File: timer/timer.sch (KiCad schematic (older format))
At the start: 1 part, among them P1 CONN_02X30

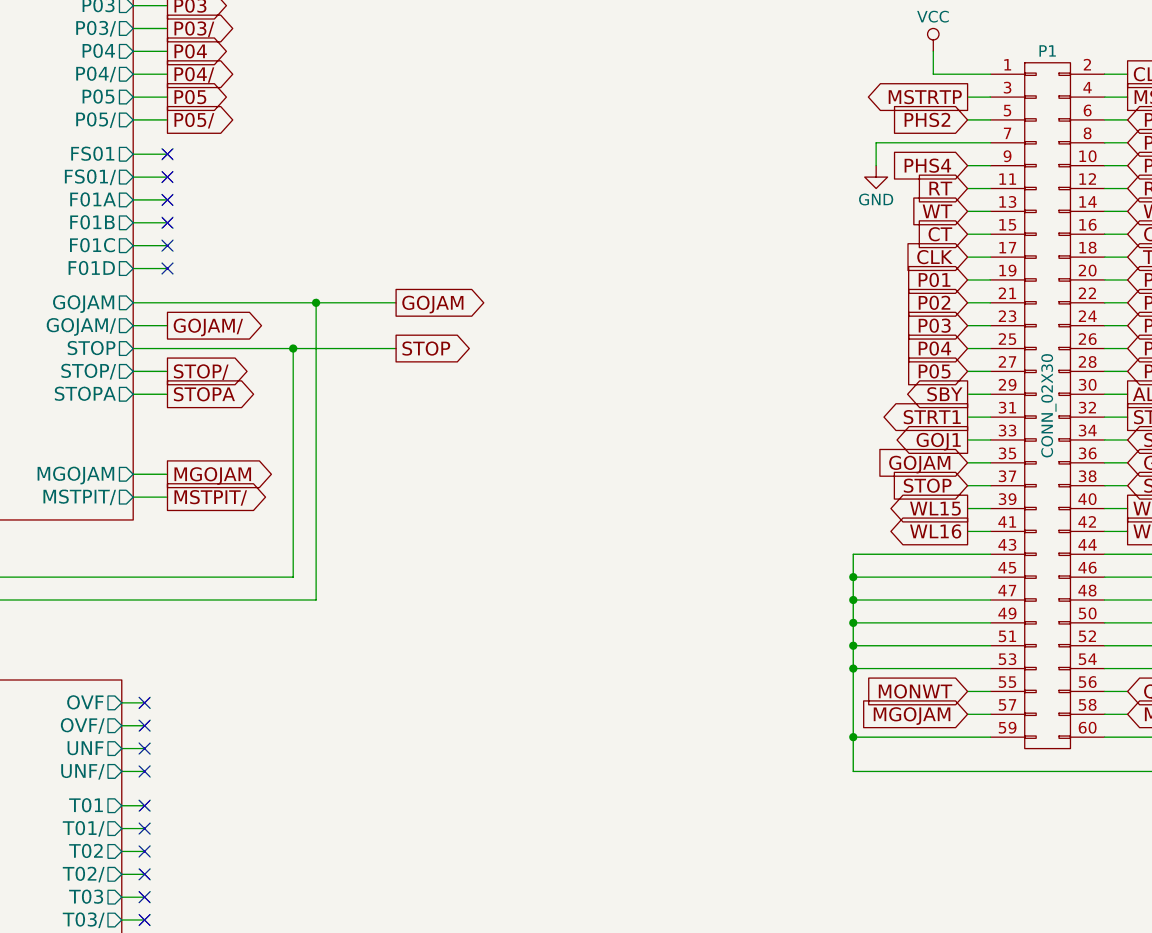
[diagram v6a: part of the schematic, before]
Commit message: Added the entire scaler module! Didn't flesh out the I/O much, I'll do that as needed. Also, the clock divider's labeling here is different from the one in the timer module, which is consistent with the original schematics. If I merge these two modules later, I'll have to figure out what to do there.
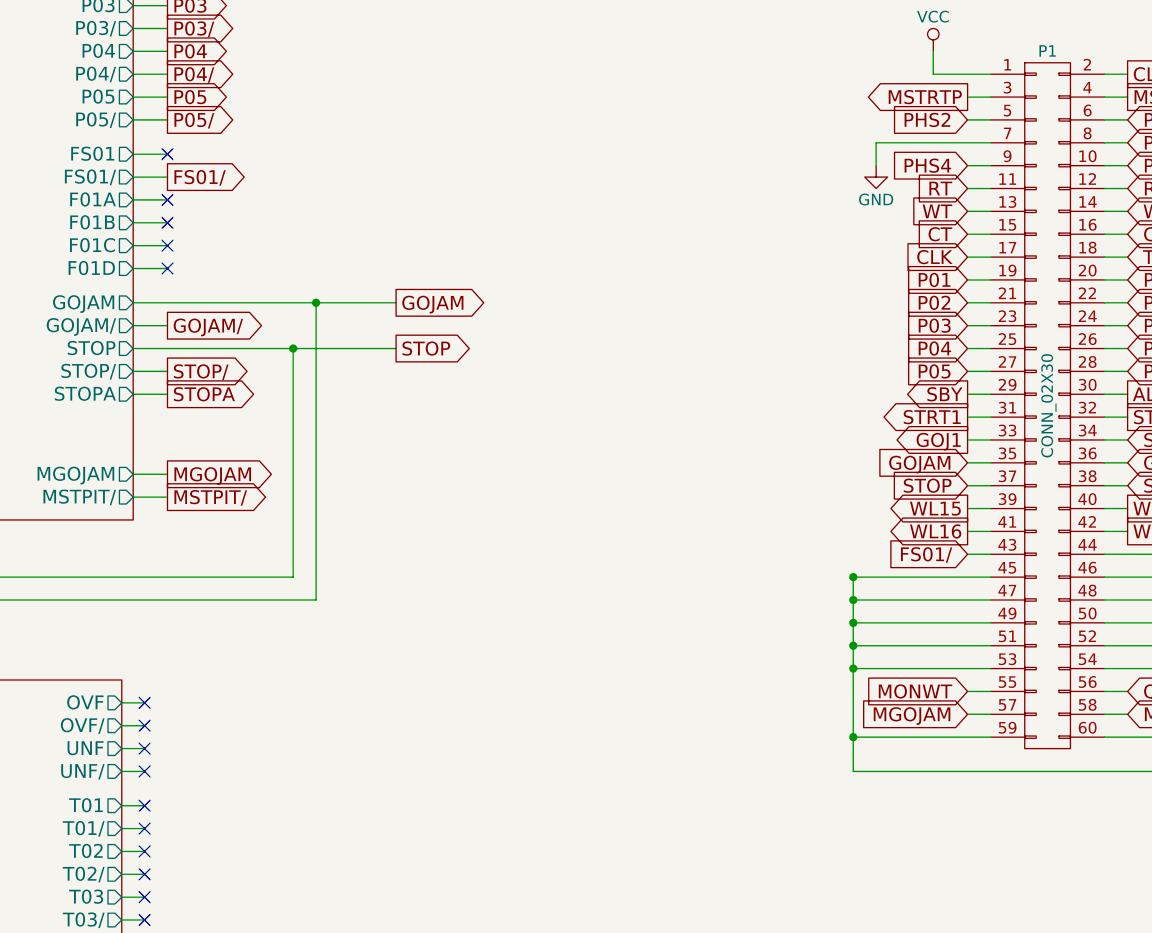
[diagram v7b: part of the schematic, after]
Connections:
- net GND: no longer P1.43 (P43)
- new net FS01/: P1.43 (P43)
- no-connect marks 58 -> 57
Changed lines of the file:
@@
 	6400 2850 6550 2850
 NoConn ~ 6550 2350
-NoConn ~ 6550 2450
 NoConn ~ 6550 2550
 NoConn ~ 6550 2650
@@
 	11300 4900 10650 4900
 Connection ~ 11300 4900
-Wire Wire Line
-	10150 4100 9550 4100
 Wire Wire Line
 	10150 4200 9550 4200
@@
 NoConn ~ 6450 5050
 Wire Wire Line
-	9550 5050 9550 4100
-Wire Wire Line
 	11300 4100 11300 5100
 Text GLabel 10050 3900 0    60   Output ~ 0
@@
 Wire Wire Line
 	4550 5900 4700 5900
+Wire Wire Line
+	9550 5050 9550 4200
+Wire Wire Line
+	10150 4100 10050 4100
+Text GLabel 10050 4100 0    60   Input ~ 0
+FS01/
+Text GLabel 6550 2450 2    60   Output ~ 0
+FS01/
 $EndSCHEMATC

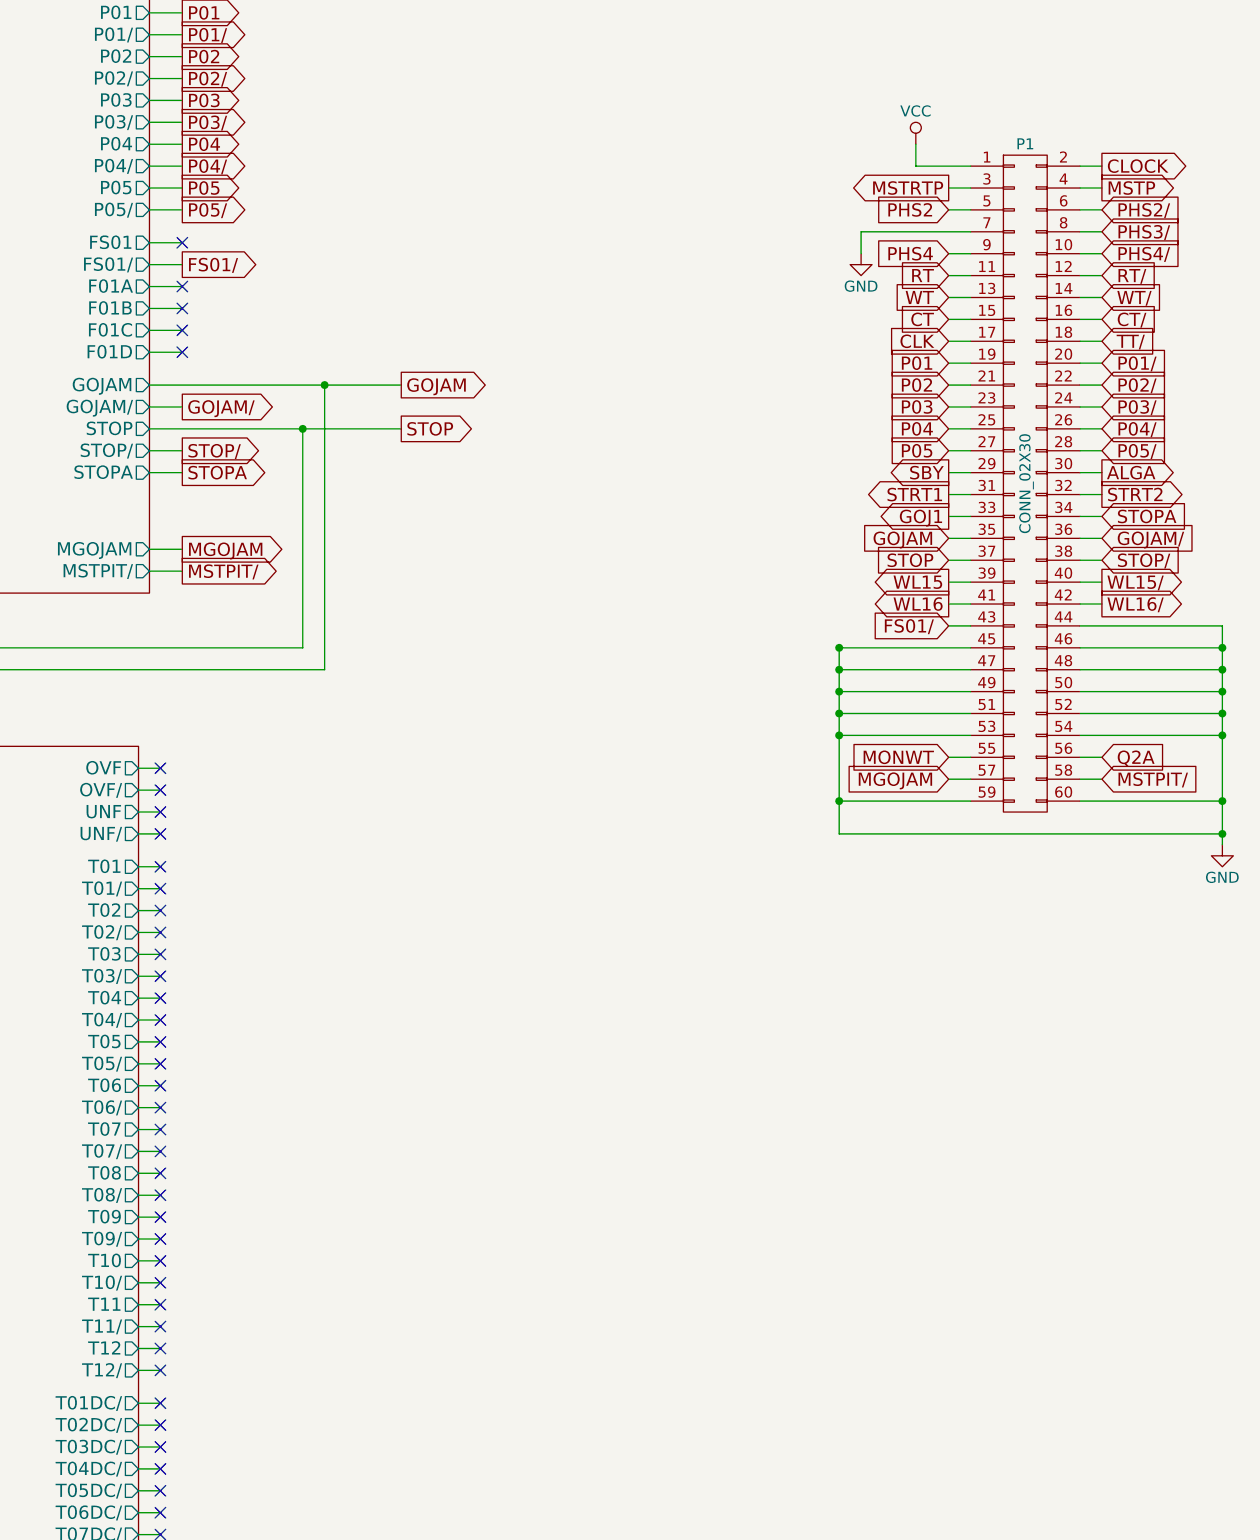
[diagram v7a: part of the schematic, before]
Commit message: Filled out the rest of page A03-1. At the very least, it appears to be properly handling the GOJAM condition. Haven't looked much at non-GOJAM behavior. I also exposed T01..T12 and T01/..T12/ as outputs of the timer module. I'm going to need a bigger (or another) connector there soon
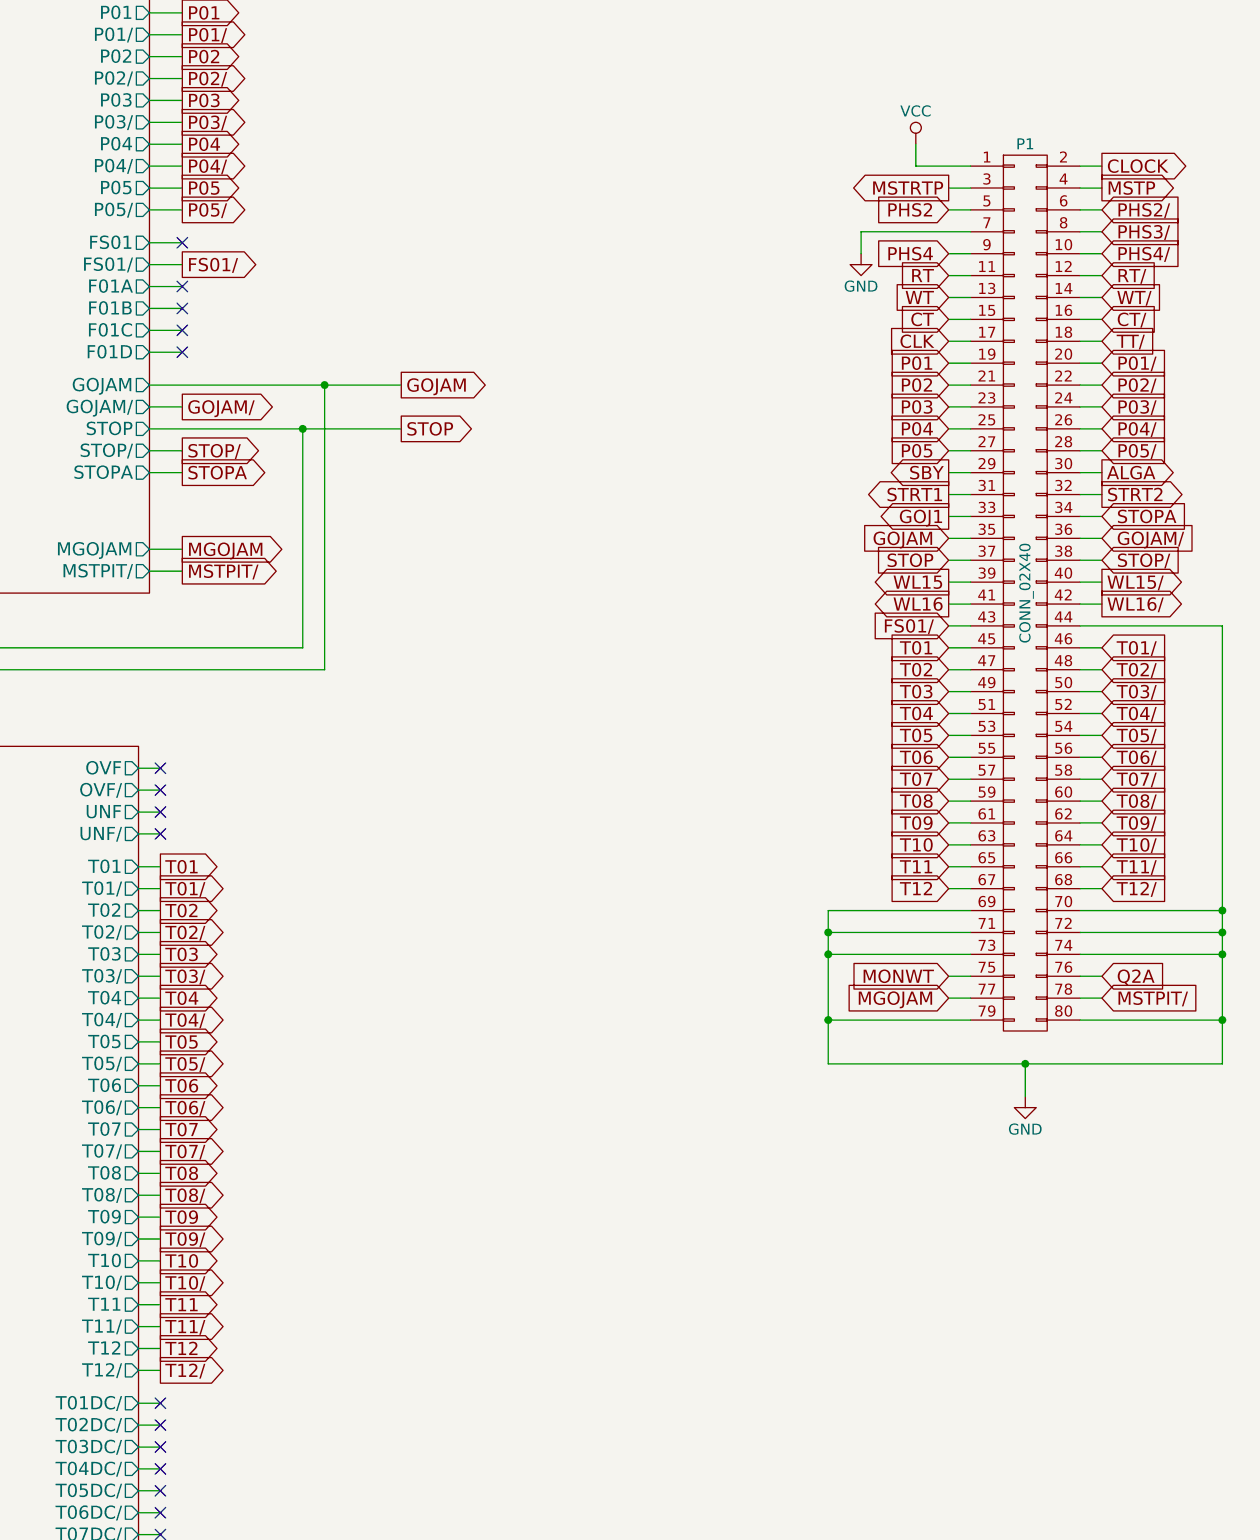
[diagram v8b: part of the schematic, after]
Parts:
- removed P1: CONN_02X30, symbol CONN_02X30
- added P1: CONN_02X40, symbol CONN_02X40
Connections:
- net ALGA: now also P1.30 (P30)
- net CLK: now also P1.17 (P17)
- net CLOCK: now also P1.2 (P2)
- net CT: now also P1.15 (P15)
- net CT/: now also P1.16 (P16)
- net FS01/: now also P1.43 (P43)
- net GND: now also P1.44 (P44), P1.69 (P69), P1.7 (P7), P1.70 (P70), P1.71 (P71), P1.72 (P72), P1.73 (P73), P1.74 (P74), P1.79 (P79), P1.80 (P80)
- net GOJ1: now also P1.33 (P33)
- net GOJAM: now also P1.35 (P35)
- net GOJAM/: now also P1.36 (P36)
- net MGOJAM: now also P1.77 (P77)
- net MONWT: now also P1.75 (P75)
- net MSTP: now also P1.4 (P4)
- net MSTPIT/: now also P1.78 (P78)
- net MSTRTP: now also P1.3 (P3)
- net P01: now also P1.19 (P19)
- net P01/: now also P1.20 (P20)
- net P02: now also P1.21 (P21)
- net P02/: now also P1.22 (P22)
- net P03: now also P1.23 (P23)
- net P03/: now also P1.24 (P24)
- net P04: now also P1.25 (P25)
- net P04/: now also P1.26 (P26)
- net P05: now also P1.27 (P27)
- net P05/: now also P1.28 (P28)
- net PHS2: now also P1.5 (P5)
- net PHS2/: now also P1.6 (P6)
- net PHS3/: now also P1.8 (P8)
- net PHS4: now also P1.9 (P9)
- net PHS4/: now also P1.10 (P10)
- net Q2A: now also P1.76 (P76)
- net RT: now also P1.11 (P11)
- net RT/: now also P1.12 (P12)
- net SBY: now also P1.29 (P29)
- net STOP: now also P1.37 (P37)
- net STOP/: now also P1.38 (P38)
- net STOPA: now also P1.34 (P34)
- net STRT1: now also P1.31 (P31)
- net STRT2: now also P1.32 (P32)
- net TT/: now also P1.18 (P18)
- net VCC: now also P1.1 (P1)
- net WL15: now also P1.39 (P39)
- net WL15/: now also P1.40 (P40)
- net WL16: now also P1.41 (P41)
- net WL16/: now also P1.42 (P42)
- net WT: now also P1.13 (P13)
- net WT/: now also P1.14 (P14)
- new net T01: P1.45 (P45)
- new net T01/: P1.46 (P46)
- new net T02: P1.47 (P47)
- new net T02/: P1.48 (P48)
- new net T03: P1.49 (P49)
- new net T03/: P1.50 (P50)
- new net T04: P1.51 (P51)
- new net T04/: P1.52 (P52)
- new net T05: P1.53 (P53)
- new net T05/: P1.54 (P54)
- new net T06: P1.55 (P55)
- new net T06/: P1.56 (P56)
- new net T07: P1.57 (P57)
- new net T07/: P1.58 (P58)
- new net T08: P1.59 (P59)
- new net T08/: P1.60 (P60)
- new net T09: P1.61 (P61)
- new net T09/: P1.62 (P62)
- new net T10: P1.63 (P63)
- new net T10/: P1.64 (P64)
- new net T11: P1.65 (P65)
- new net T11/: P1.66 (P66)
- new net T12: P1.67 (P67)
- new net T12/: P1.68 (P68)
- no-connect marks 57 -> 33
